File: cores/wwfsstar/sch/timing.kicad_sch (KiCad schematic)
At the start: 1 part, among them X1 24. 000 MHz

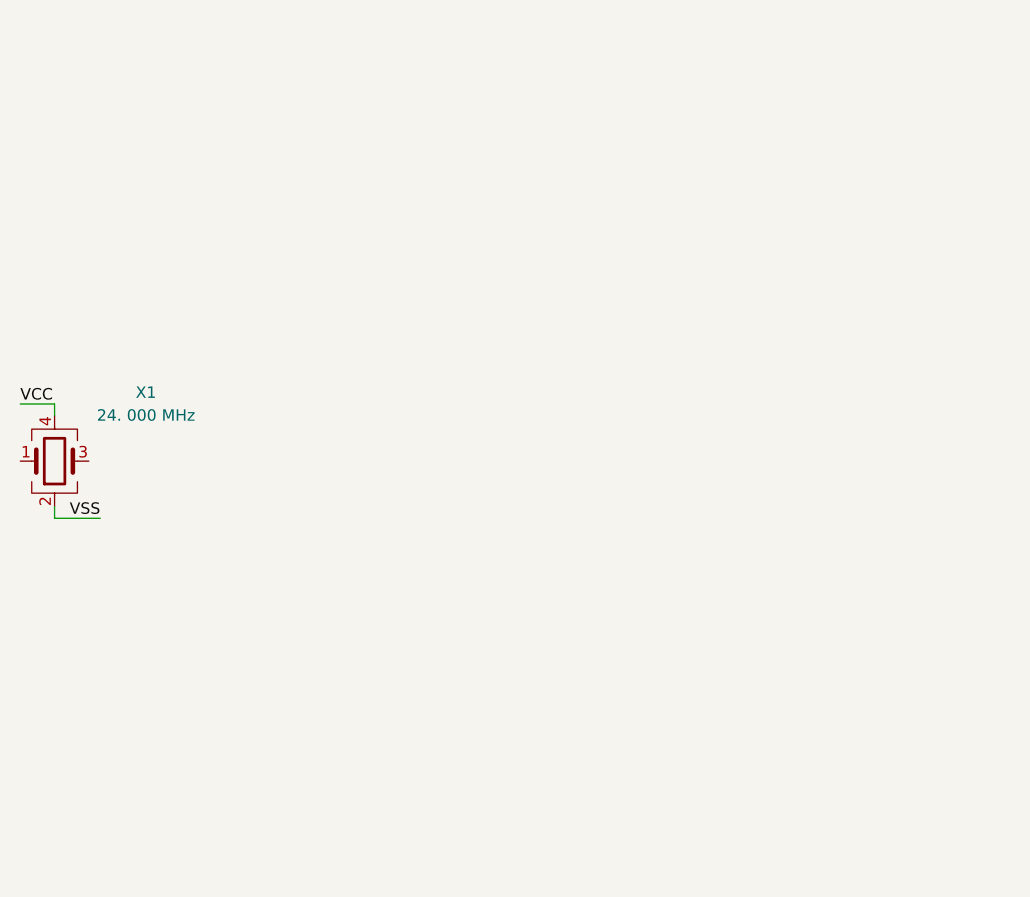
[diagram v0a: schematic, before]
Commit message: wwfsstar sch: working on scroll page
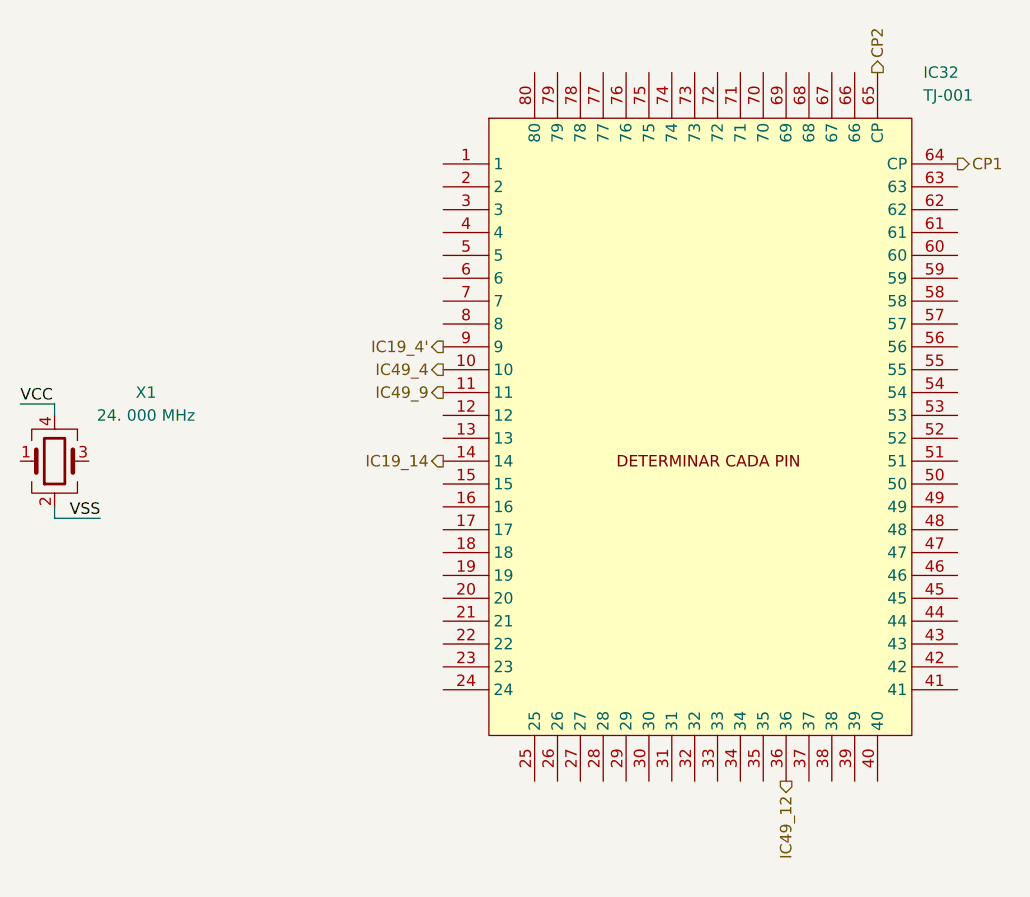
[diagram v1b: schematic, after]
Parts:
- added IC32: TJ-001, symbol technos:TJ-001
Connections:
- new net CP1: IC32.64 (CP)
- new net CP2: IC32.65 (CP)
- new net IC19_14: IC32.14
- new net IC19_4': IC32.9
- new net IC49_12: IC32.36
- new net IC49_4: IC32.10
- new net IC49_9: IC32.11

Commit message: wwfsstar: io edits
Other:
- company: (none) -> JOTEGO
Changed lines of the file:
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@@
 	(generator_version "8.0")
 	(paper "A3")
+	(title_block
+		(company "JOTEGO")
+	)
 	(wire
 		(pts
